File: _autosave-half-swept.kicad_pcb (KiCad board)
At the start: 2 copper layers, 109 x 86.9 mm, 23 parts, among them J2 AudioJack4dpb, SW1 SW_Push, SW10 SW_Push, SW11 SW_Push, SW12 SW_Push, SW13 SW_Push, SW14 SW_Push, SW15 SW_Push, SW16 SW_Push, SW17 SW_Push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

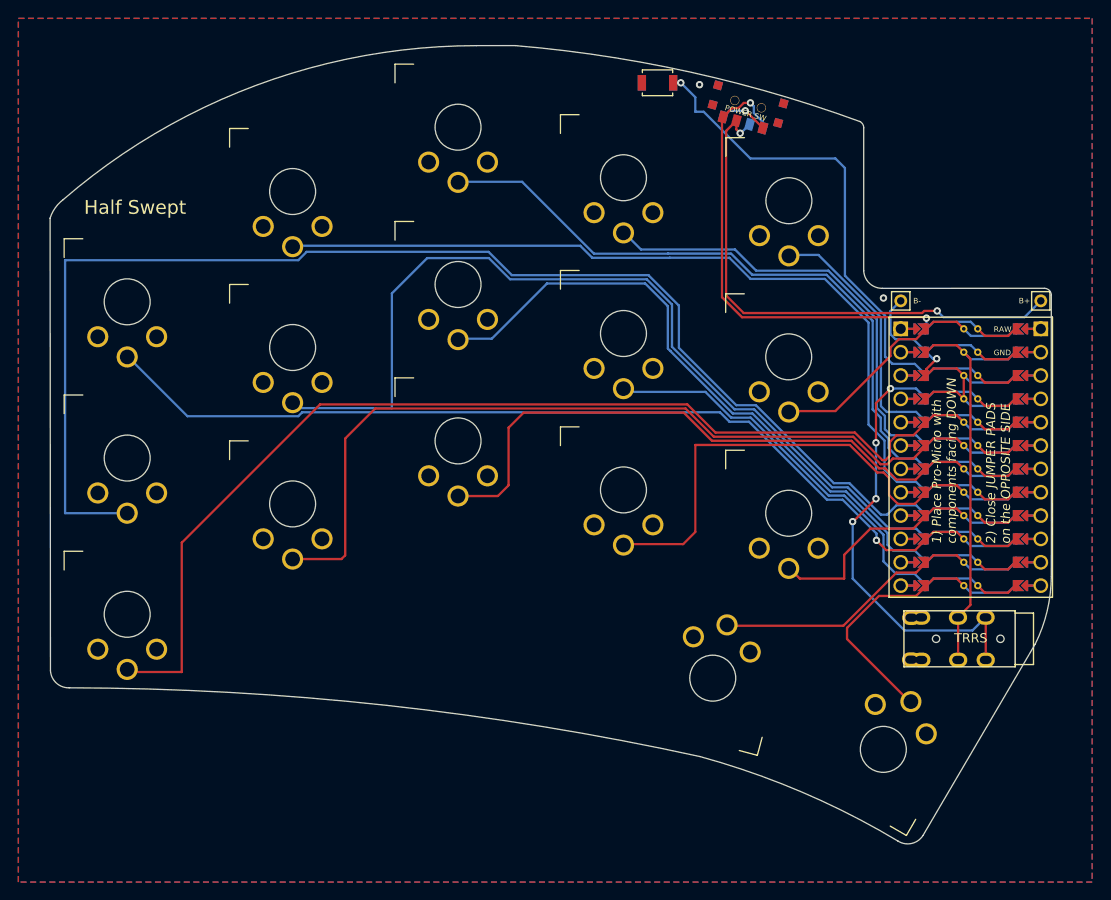
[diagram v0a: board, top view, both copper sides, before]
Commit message: (fix) routes and pcb edge cut
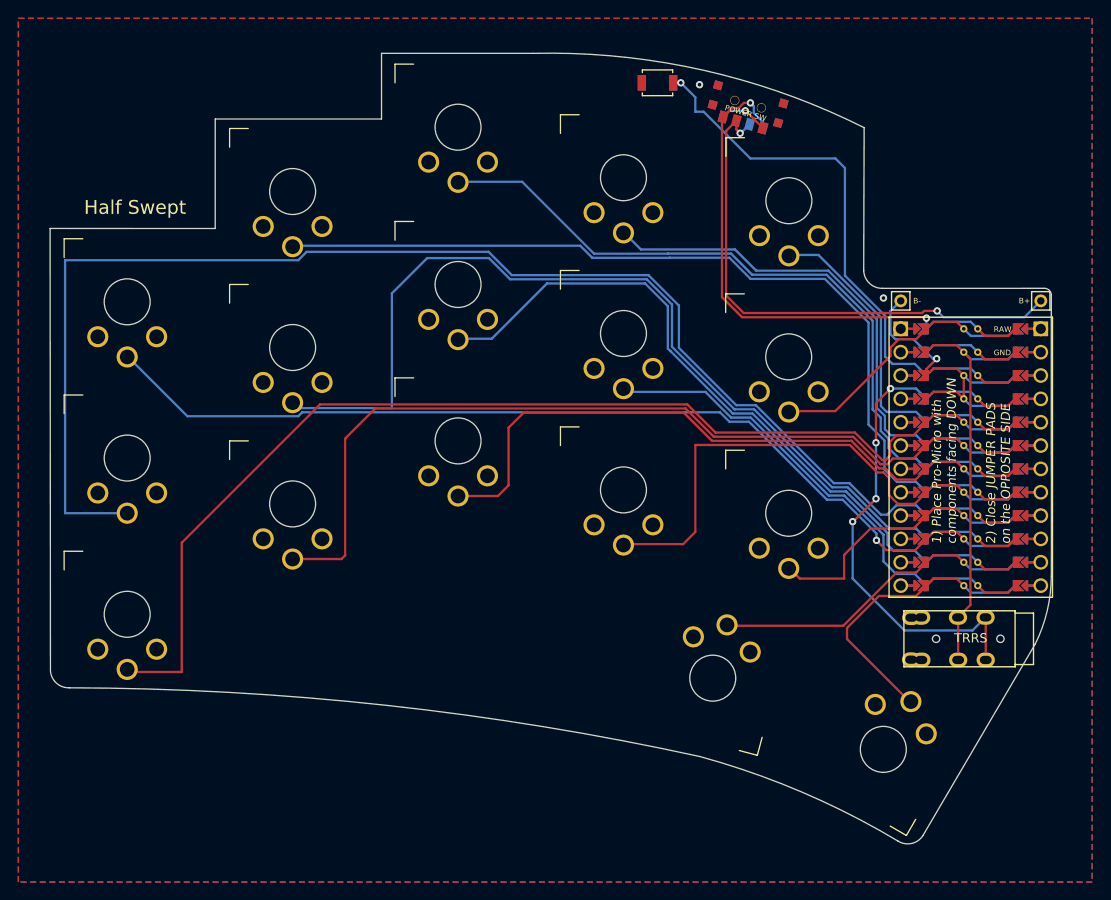
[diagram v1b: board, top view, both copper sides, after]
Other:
- board size 109 x 86.9 mm -> 109 x 86 mm
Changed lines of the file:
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@@
   (gr_arc (start 126.885 44.612) (mid 127.41533 44.83167) (end 127.635 45.362)
     (stroke (width 0.05) (type solid)) (layer "Edge.Cuts"))
-  (gr_line (start 18.690055 36.976702) (end 18.730254 86.245024)
-    (stroke (width 0.05) (type solid)) (layer "Edge.Cuts"))
-  (gr_arc (start 106.78729 26.456889) (mid 107.104079 26.733645) (end 107.222045 27.137419)
+  (gr_line (start 18.690055 38.1) (end 18.730254 86.245024)
     (stroke (width 0.05) (type solid)) (layer "Edge.Cuts"))
   (gr_arc (start 89.409134 95.561946) (mid 100.486488 99.421597) (end 110.938 104.748)
     (stroke (width 0.05) (type solid)) (layer "Edge.Cuts"))
-  (gr_arc (start 18.690055 36.976702) (mid 19.246929 35.858882) (end 20.117 34.963)
-    (stroke (width 0.05) (type solid)) (layer "Edge.Cuts"))
   (gr_arc (start 109.257002 44.614917) (mid 107.844534 44.065716) (end 107.222001 42.683999)
     (stroke (width 0.05) (type solid)) (layer "Edge.Cuts"))
-  (gr_arc (start 69.291777 18.200679) (mid 88.315879 21.073764) (end 106.78729 26.456889)
+  (gr_arc (start 71.288781 19.044958) (mid 89.774316 20.878987) (end 107.26706 27.130593)
     (stroke (width 0.05) (type solid)) (layer "Edge.Cuts"))
   (gr_arc (start 113.67 104.149265) (mid 112.428995 105.01898) (end 110.938 104.748)
@@
   (gr_line (start 127.635 45.362) (end 127.635 62.484)
     (stroke (width 0.05) (type solid)) (layer "Edge.Cuts"))
-  (gr_line (start 107.222001 42.683999) (end 107.222045 27.137419)
+  (gr_line (start 107.222001 42.683999) (end 107.26706 27.130593)
     (stroke (width 0.05) (type solid)) (layer "Edge.Cuts"))
   (gr_line (start 109.257002 44.614917) (end 126.885 44.612)
-    (stroke (width 0.05) (type solid)) (layer "Edge.Cuts"))
-  (gr_arc (start 20.117 34.963) (mid 41.093524 22.531455) (end 65.090389 18.206139)
     (stroke (width 0.05) (type solid)) (layer "Edge.Cuts"))
   (gr_line (start 125.888304 83.312) (end 113.67 104.149265)
@@
   (gr_arc (start 127.635 75.98785) (mid 127.177913 79.749197) (end 125.888304 83.312)
     (stroke (width 0.05) (type solid)) (layer "Edge.Cuts"))
-  (gr_line (start 69.291777 18.200679) (end 65.090389 18.206139)
-    (stroke (width 0.05) (type solid)) (layer "Edge.Cuts"))
   (gr_line (start 127.635 62.484) (end 127.647 69.85)
     (stroke (width 0.05) (type solid)) (layer "Edge.Cuts"))
   (gr_line (start 127.647 69.85) (end 127.635 75.98785)
     (stroke (width 0.05) (type solid)) (layer "Edge.Cuts"))
+  (gr_line (start 18.690055 38.1) (end 36.656634 38.103657)
+    (stroke (width 0.05) (type default)) (layer "Edge.Cuts"))
+  (gr_line (start 36.659619 26.186848) (end 54.754406 26.186848)
+    (stroke (width 0.05) (type default)) (layer "Edge.Cuts"))
+  (gr_line (start 36.659619 26.186848) (end 36.659619 26.186848)
+    (stroke (width 0.05) (type default)) (layer "Edge.Cuts"))
+  (gr_line (start 36.659619 26.186848) (end 36.659619 26.186848)
+    (stroke (width 0.05) (type default)) (layer "Edge.Cuts"))
+  (gr_line (start 54.754406 19.044958) (end 71.288781 19.044958)
+    (stroke (width 0.05) (type default)) (layer "Edge.Cuts"))
+  (gr_line (start 54.754406 26.186848) (end 54.754406 19.044958)
+    (stroke (width 0.05) (type default)) (layer "Edge.Cuts"))
+  (gr_line (start 36.656634 38.103657) (end 36.659619 26.186848)
+    (stroke (width 0.05) (type default)) (layer "Edge.Cuts"))
   (gr_text "RAW" (at 116.40097 49.0728) (layer "B.SilkS")
     (effects (font (size 0.6 0.6) (thickness 0.12)) (justify left mirror))
